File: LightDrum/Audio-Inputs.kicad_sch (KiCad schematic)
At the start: 37 parts, among them J201 XLR3, J202 SJ-43515RS-SMT-TR

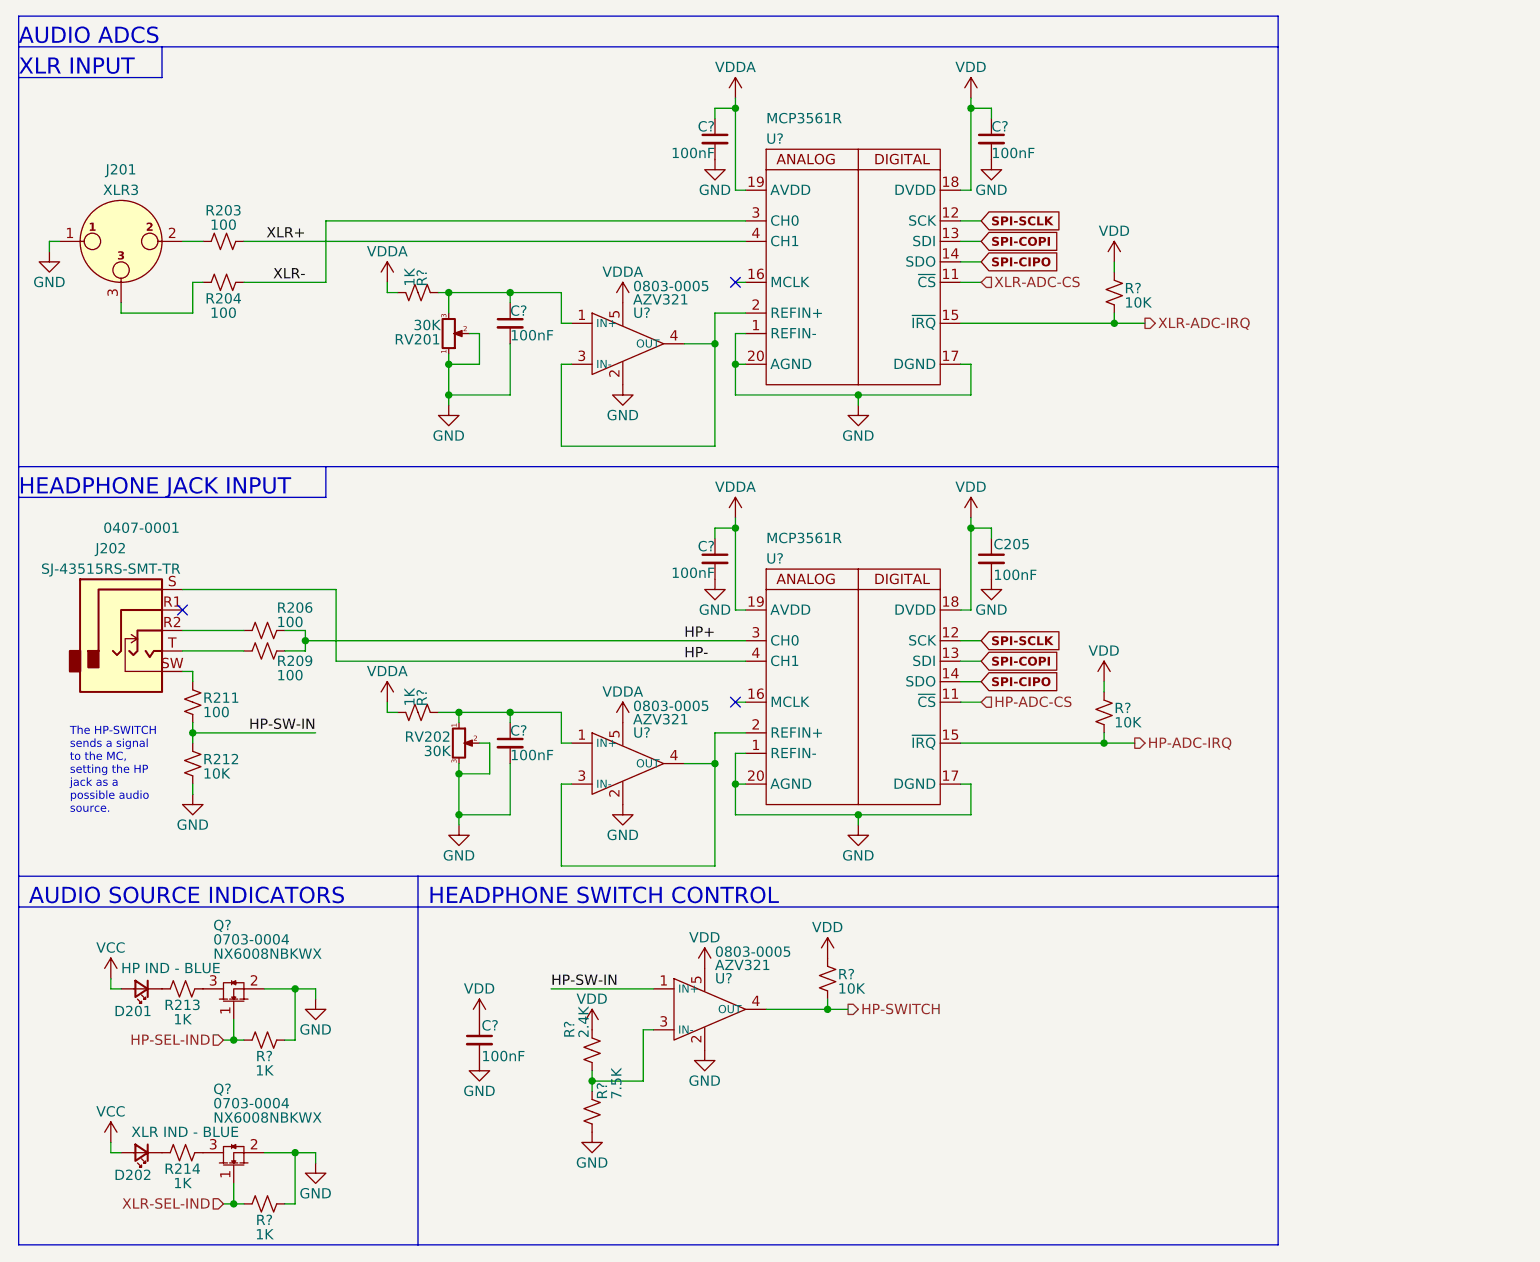
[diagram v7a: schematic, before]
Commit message: Replace old MOSFETs with a more compact package
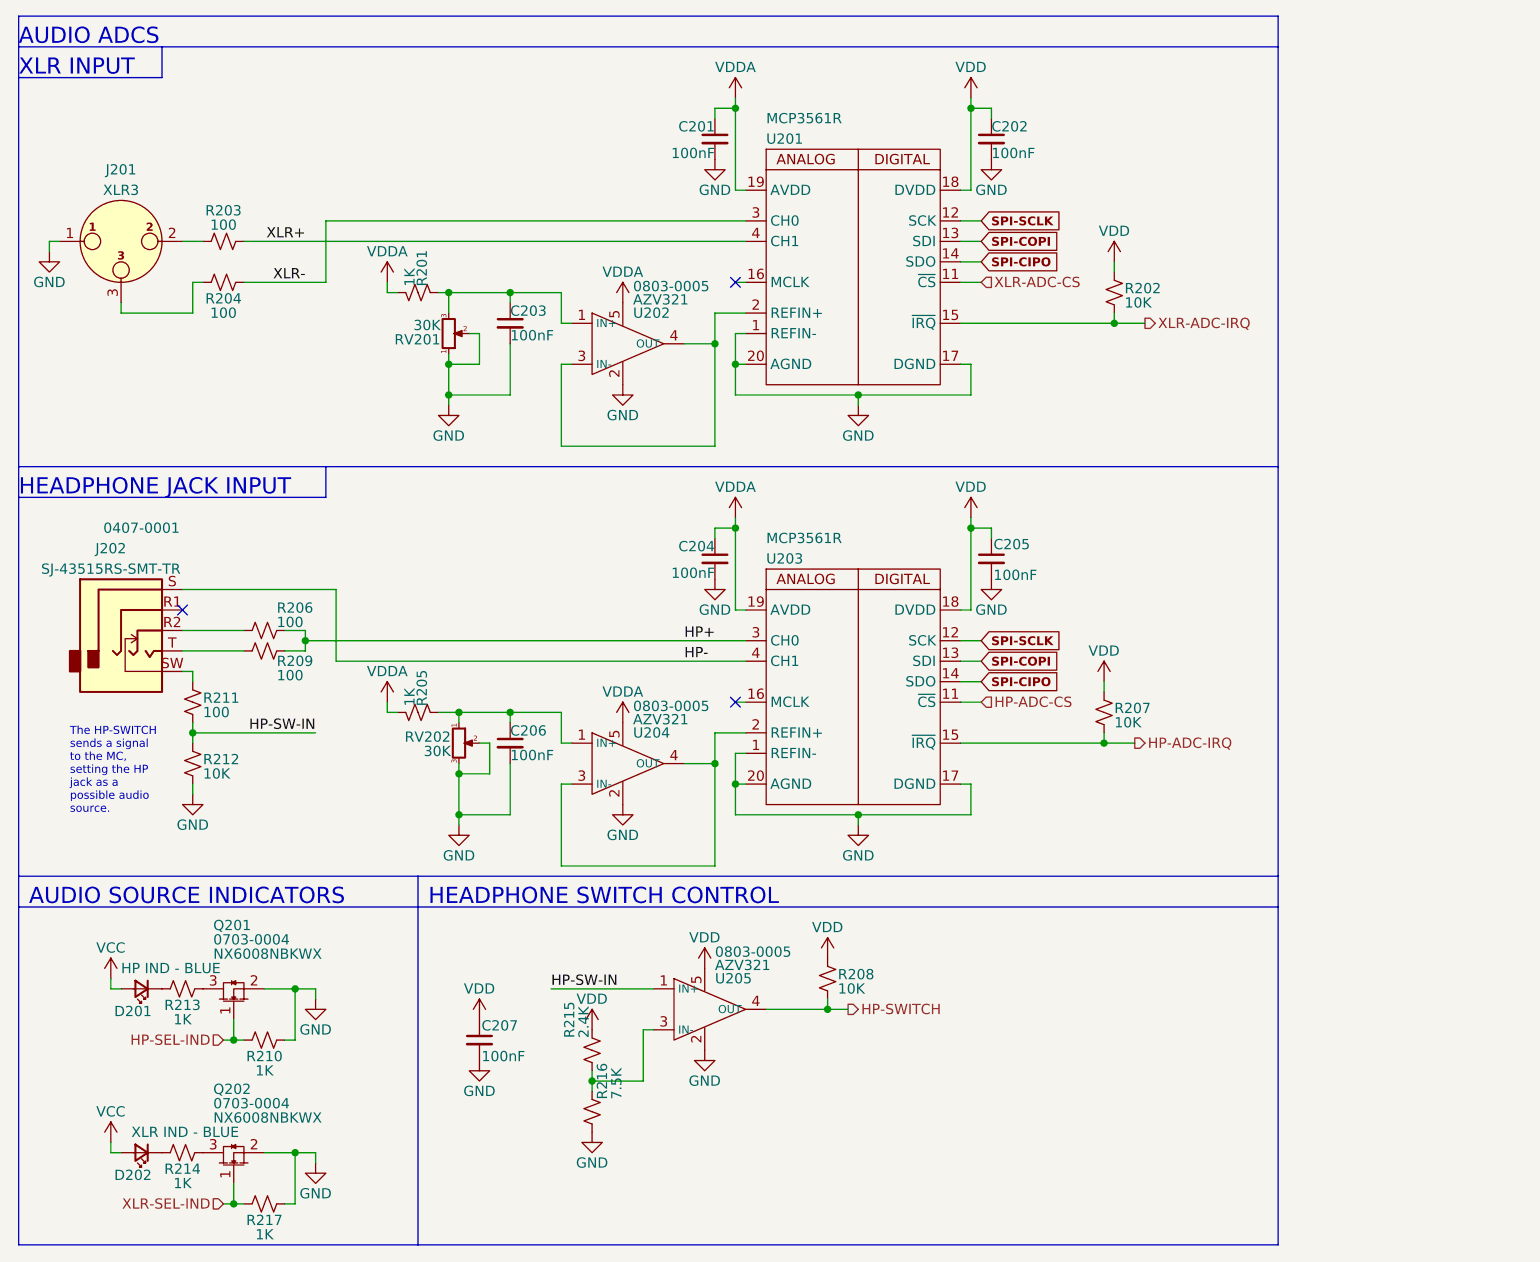
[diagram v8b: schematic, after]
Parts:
- gave numbers to parts that had none: 22
